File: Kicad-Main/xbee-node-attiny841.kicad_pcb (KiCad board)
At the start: 2 copper layers, 58.5 x 58.5 mm, 41 parts, among them P10 CONN_1, P11 CONN_1, P12 CONN_1, P13 CONN_1, P14 CONN_1, P15 CONN_1, P16 CONN_1, P17 CONN_1, P18 CONN_1, P2 XBee Adaptor, P3 Test, P4 Battery, P5 XBee-ext-1, P6 XBee-ext-2, P7 CONN_1, P8 CONN_1, P9 CONN_1, Q2 S9014, Q3 2N7000, U1 ATTINY84-S, U2 MAX952ESA, U3 TPS77033

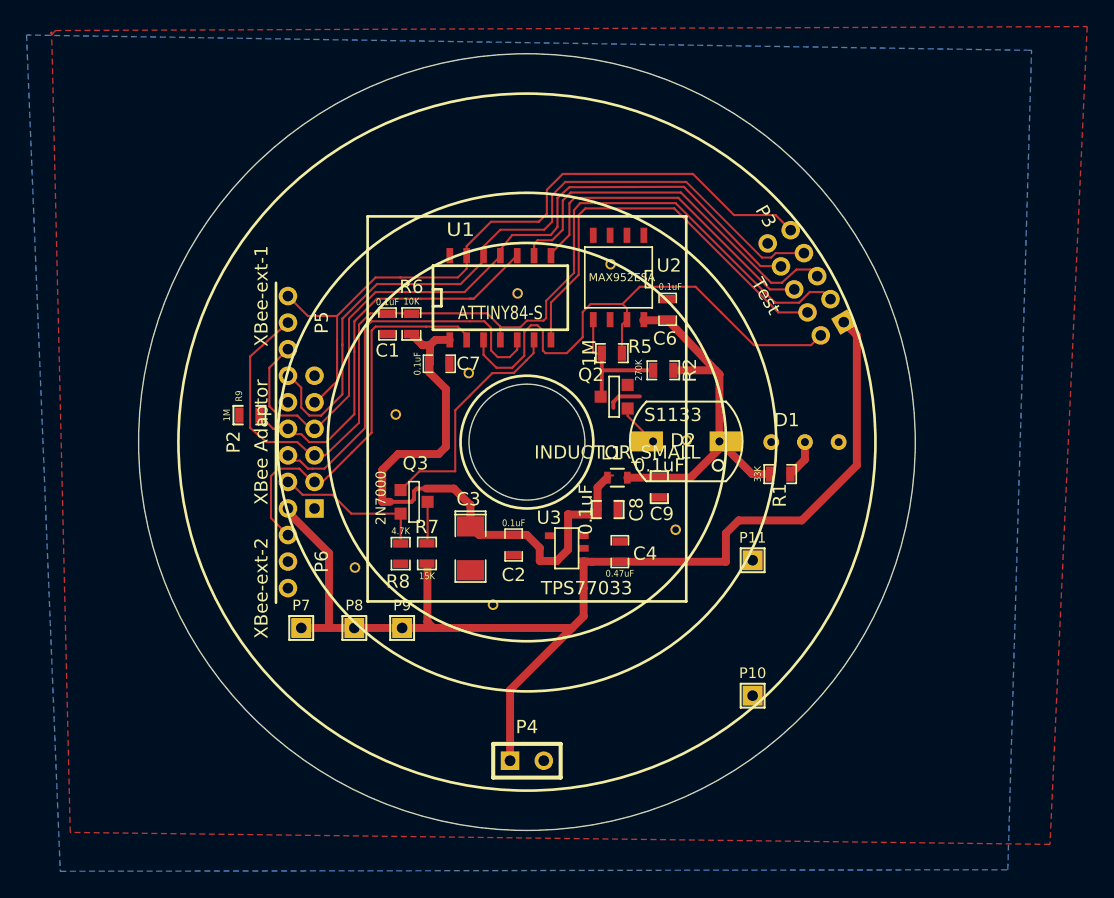
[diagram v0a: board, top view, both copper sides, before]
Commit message: Move some components away from centre to leave room for a shaft housing.
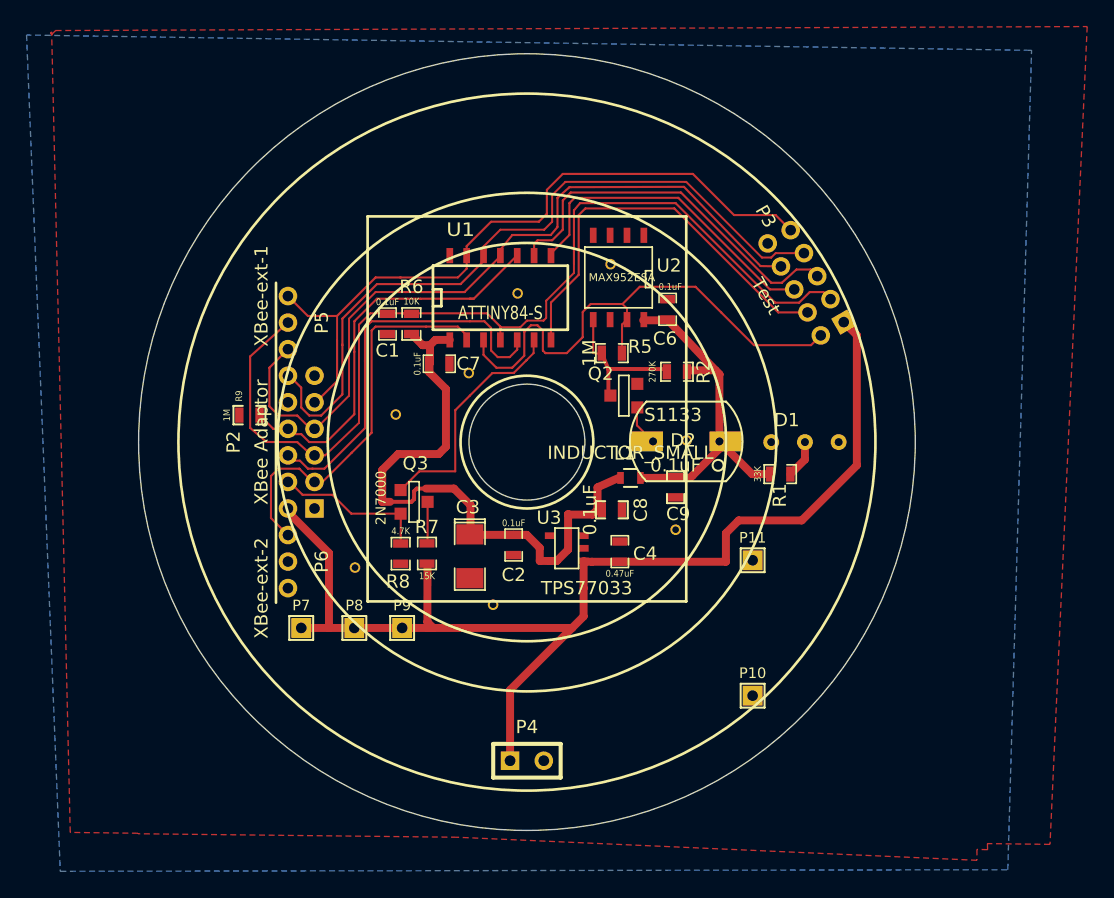
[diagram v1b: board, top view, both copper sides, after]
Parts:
- moved C9 1.23 mm to (211.2, 103.4)
- moved R2 1.04 mm to (211.3, 94.7)
- moved L1 0.99 mm to (207.8, 102.7)
- moved Q2 0.73 mm to (207.3, 96.5)
- moved C3 0.60 mm to (195.7, 108.6)
- moved C8 0.32 mm to (206.4, 105.1)
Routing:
- net (no net): track 2.61 -> 0.00 mm
- net /VDDA: track 29.4 -> 27.1 mm
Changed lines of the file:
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@@
-(kicad_pcb (version 4) (host pcbnew "(2014-08-05 BZR 5054)-product")
+(kicad_pcb (version 4) (host pcbnew 4.0.2-4+6225~38~ubuntu14.04.1-stable)
   (general
     (links 85)
-    (no_connects 5)
-    (area 170.699999 70.699999 229.300001 129.300001)
+    (no_connects 6)
+    (area 162.31 68.7 242.200001 132.330001)
     (thickness 1.6)
     (drawings 11)
-    (tracks 336)
+    (tracks 332)
     (zones 0)
     (modules 41)
@@
   )
   (setup
-    (last_trace_width 0.3)
+    (last_trace_width 0.16)
     (user_trace_width 0.3)
     (user_trace_width 0.6)
@@
   )
   (module SMD_Packages:SM1206POL (layer F.Cu)
-    (at 195.75 108 270)
+    (at 195.7 108.6 270)
     (attr smd)
     (fp_text reference C3 (at -3.7 0.15 360) (layer F.SilkS)
@@
   )
   (module SMD_Packages:SM0603_Resistor (layer F.Cu)
-    (at 210.27 94.59 180)
+    (at 211.3 94.7 180)
     (attr smd)
     (fp_text reference R2 (at -2 0 270) (layer F.SilkS)
@@
   )
   (module SMD_Packages:SOT23EBC (layer F.Cu)
-    (at 206.57 96.58 270)
+    (at 207.3 96.5 270)
     (descr "Module CMS SOT23 Transistore EBC")
     (tags "CMS SOT")
@@
   )
   (module SMD_Packages:SMD-0603_c (layer F.Cu)
-    (at 206.08 105.08)
+    (at 206.4 105.1)
     (attr smd)
     (fp_text reference C8 (at 2.17 0 90) (layer F.SilkS)
@@
   )
   (module SMD_Packages:SMD-0603_c (layer F.Cu)
-    (at 209.97 103.4 270)
+    (at 211.2 103.4 270)
     (attr smd)
     (fp_text reference C9 (at 2.01 -0.19 360) (layer F.SilkS)
@@
   )
   (module Resistors_SMD:R_0603 (layer F.Cu)
-    (at 206.81 102.68 180)
+    (at 207.8 102.7 180)
     (descr "Resistor SMD 0603, reflow soldering, Vishay (see dcrcw.pdf)")
     (tags "resistor 0603")
@@
   (gr_line (start 188 112) (end 212 112) (angle 90) (layer F.SilkS) (width 0.2))
   (gr_circle (center 200 100) (end 204.25 101) (layer Edge.Cuts) (width 0.1))
-  (segment (start 208.51 96.56) (end 206.93 96.56) (width 0.3) (layer F.Cu) (net 0))
-  (segment (start 206.51 96.98) (end 206.51 97.42) (width 0.3) (layer F.Cu) (net 0))
-  (segment (start 206.93 96.56) (end 206.51 96.98) (width 0.3) (layer F.Cu) (net 0))
   (segment (start 184 103) (end 183.86 103) (width 0.16) (layer F.Cu) (net 1))
   (segment (start 183.86 103) (end 182.86 102) (width 0.16) (layer F.Cu) (net 1))
@@
   (segment (start 192.7 92.7) (end 192.138 92.7) (width 0.6) (layer F.Cu) (net 12))
   (segment (start 205.318 105.08) (end 205.318 103.41) (width 0.6) (layer F.Cu) (net 12))
-  (segment (start 205.318 103.41) (end 206.048 102.68) (width 0.6) (layer F.Cu) (net 12))
+  (segment (start 205.318 103.41) (end 206.9 102.7) (width 0.6) (layer F.Cu) (net 12))
   (segment (start 203.1 105.46) (end 204.938 105.46) (width 0.6) (layer F.Cu) (net 12))
   (segment (start 204.938 105.46) (end 205.318 105.08) (width 0.6) (layer F.Cu) (net 12))
-  (segment (start 206 102.512) (end 206.5 102.512) (width 0.15) (layer F.Cu) (net 12))
   (segment (start 203.1 108.1) (end 203.1 105.46) (width 0.6) (layer F.Cu) (net 12))
   (segment (start 203.1 105.46) (end 203.1 105.412) (width 0.6) (layer F.Cu) (net 12))
@@
   (segment (start 195.738 104.738) (end 194.5 103.5) (width 0.6) (layer F.Cu) (net 12))
   (segment (start 195.75 104.738) (end 195.738 104.738) (width 0.6) (layer F.Cu) (net 12))
-  (segment (start 205.638 94.61) (end 205.638 96.846) (width 0.3) (layer F.Cu) (net 13))
-  (segment (start 205.638 93.3) (end 205.638 94.61) (width 0.3) (layer F.Cu) (net 13))
+  (segment (start 206.138 94.51) (end 206.138 96.746) (width 0.3) (layer F.Cu) (net 13))
+  (segment (start 205.638 93.3) (end 206.138 94.51) (width 0.3) (layer F.Cu) (net 13))
   (segment (start 205.47 93.35) (end 204.99 93.29) (width 0.16) (layer F.Cu) (net 13))
   (segment (start 204.99 93.29) (end 204.995 90.775) (width 0.16) (layer F.Cu) (net 13))
   (segment (start 205.47 93.35) (end 205.638 93.3) (width 0.15) (layer F.Cu) (net 13))
-  (segment (start 205.638 94.59) (end 205.658 94.61) (width 0.3) (layer F.Cu) (net 13))
-  (segment (start 205.658 94.61) (end 205.7 94.61) (width 0.3) (layer F.Cu) (net 13))
-  (segment (start 205.7 94.61) (end 205.638 94.61) (width 0.3) (layer F.Cu) (net 13))
-  (segment (start 209.508 94.59) (end 205.638 94.59) (width 0.3) (layer F.Cu) (net 13))
+  (segment (start 206.138 94.49) (end 206.158 94.51) (width 0.3) (layer F.Cu) (net 13))
+  (segment (start 206.158 94.51) (end 206.2 94.51) (width 0.3) (layer F.Cu) (net 13))
+  (segment (start 206.2 94.51) (end 206.138 94.51) (width 0.3) (layer F.Cu) (net 13))
+  (segment (start 210.4 94.5) (end 206.138 94.49) (width 0.3) (layer F.Cu) (net 13))
   (segment (start 203.9 87.4) (end 203.9 82.9) (width 0.16) (layer F.Cu) (net 15))
   (segment (start 203.9 82.9) (end 204.4 82.4) (width 0.16) (layer F.Cu) (net 15))
@@
   (segment (start 220.94 101.312) (end 219.842 102.41) (width 0.6) (layer F.Cu) (net 25))
   (segment (start 220.94 100) (end 220.94 101.312) (width 0.6) (layer F.Cu) (net 25))
-  (segment (start 207.586 98.036) (end 209.5 99.95) (width 0.16) (layer F.Cu) (net 26))
-  (segment (start 207.586 97.469) (end 207.586 98.036) (width 0.16) (layer F.Cu) (net 26))
-  (segment (start 207.56 102.68) (end 212.32 102.68) (width 0.6) (layer F.Cu) (net 27))
+  (segment (start 208.286 98.736) (end 209.5 99.95) (width 0.16) (layer F.Cu) (net 26))
+  (segment (start 208.286 97.369) (end 208.286 98.736) (width 0.16) (layer F.Cu) (net 26))
+  (segment (start 208.7 102.7) (end 212.32 102.68) (width 0.6) (layer F.Cu) (net 27))
   (segment (start 212.488 102.512) (end 214.5 100.5) (width 0.6) (layer F.Cu) (net 27))
   (segment (start 212.32 102.68) (end 212.488 102.512) (width 0.6) (layer F.Cu) (net 27))
@@
   (segment (start 208.755 90.825) (end 210.625 90.825) (width 0.6) (layer F.Cu) (net 27))
   (segment (start 218.318 102.41) (end 216.96 102.41) (width 0.6) (layer F.Cu) (net 27))
-  (segment (start 211.032 94.59) (end 214.19 94.59) (width 0.6) (layer F.Cu) (net 27))
+  (segment (start 212.2 94.6) (end 214.19 94.59) (width 0.6) (layer F.Cu) (net 27))
   (segment (start 214.19 94.59) (end 214.5 94.9) (width 0.6) (layer F.Cu) (net 27))
   (segment (start 210.625 90.825) (end 214.5 94.9) (width 0.6) (layer F.Cu) (net 27))
@@
     (polygon
       (pts
-        (xy 242.2 68.7) (xy 239.4 130.3) (xy 165.6 129.4) (xy 164.204538 69.295462) (xy 164.5 69)
+        (xy 239.4 130.3) (xy 234.68425 130.242491) (xy 234.7 130.7) (xy 233.893371 130.679379) (xy 233.9 131.5)
+        (xy 194.734053 129.763284) (xy 170.7 129.5) (xy 170.698854 129.462181) (xy 165.6 129.4) (xy 164.204538 69.295462)
+        (xy 164.5 69) (xy 242.2 68.7) (xy 239.4 130.3)
       )
     )

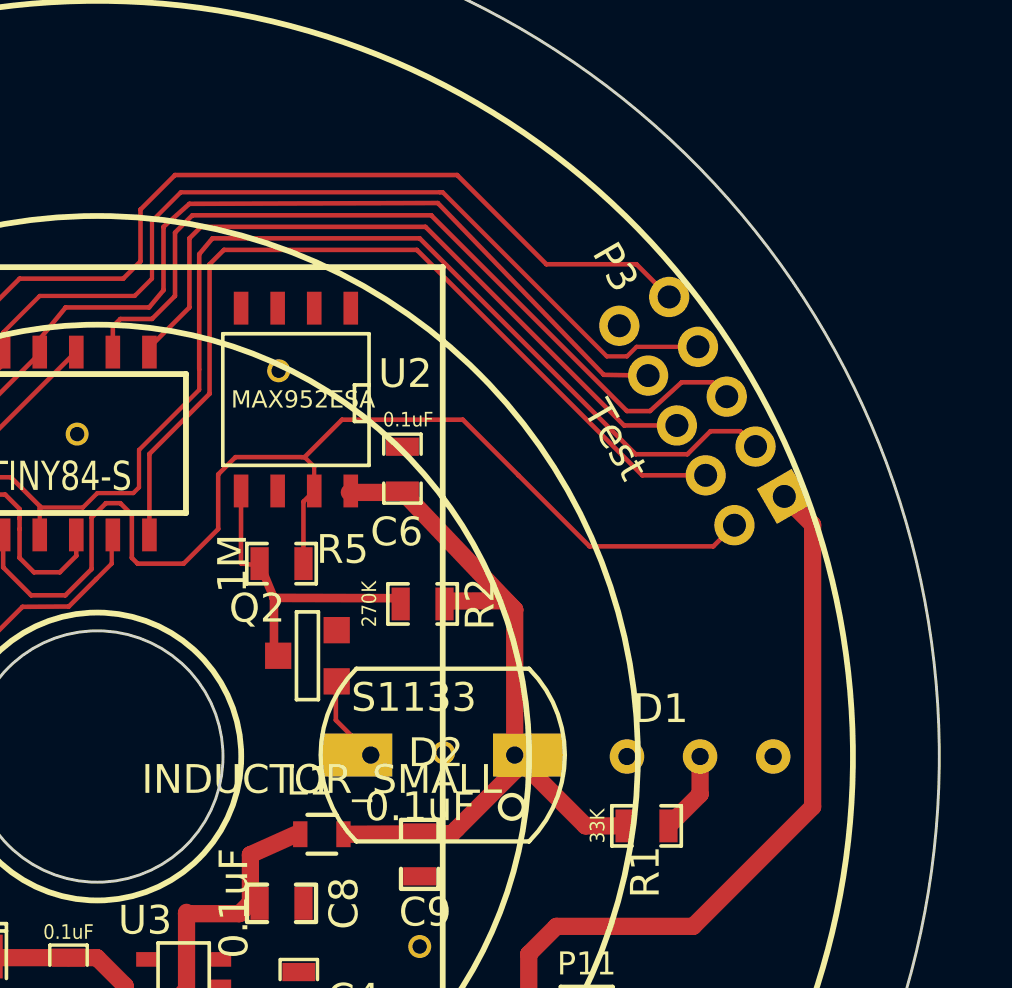
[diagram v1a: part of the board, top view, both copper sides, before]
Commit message: Change orientation of debug connector on main board to fit in housing. Update mounts to narrow down the LED mount
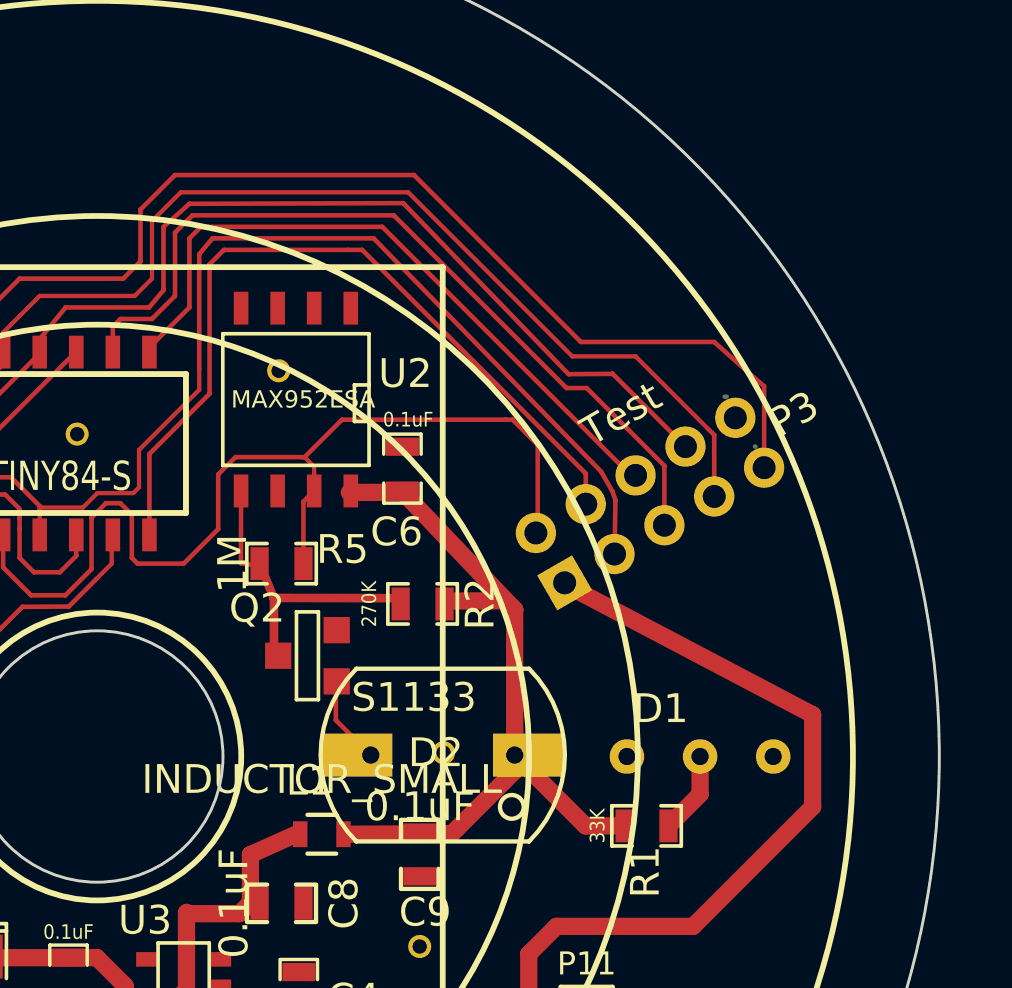
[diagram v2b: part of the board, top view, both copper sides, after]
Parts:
- moved P3 3.58 mm to (219.2, 91.1), turned to 30 degrees
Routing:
- net /On/Sleep: track 54.1 -> 61.4 mm
- net /Count: track 40.5 -> 34.6 mm
- net /Tx: track 55.9 -> 59.6 mm
- net /MOSI: track 31.0 -> 27.9 mm
- net /Reset: track 75.0 -> 72.4 mm
- net /Rx: track 59.4 -> 61.8 mm
- net /Battery: track 90.2 -> 91.7 mm

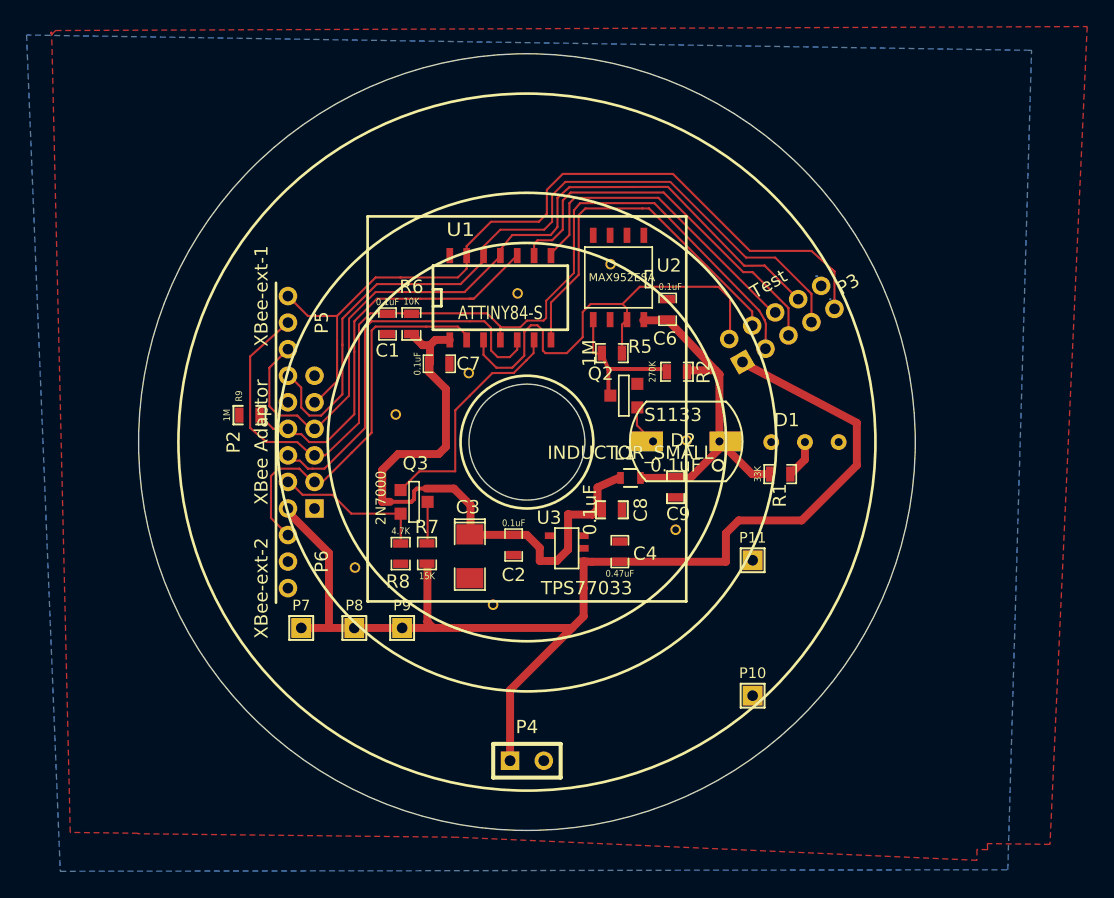
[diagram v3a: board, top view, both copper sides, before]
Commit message: Shift XBee connector on main board by 1mm to avoid housing structures. Update documentation.
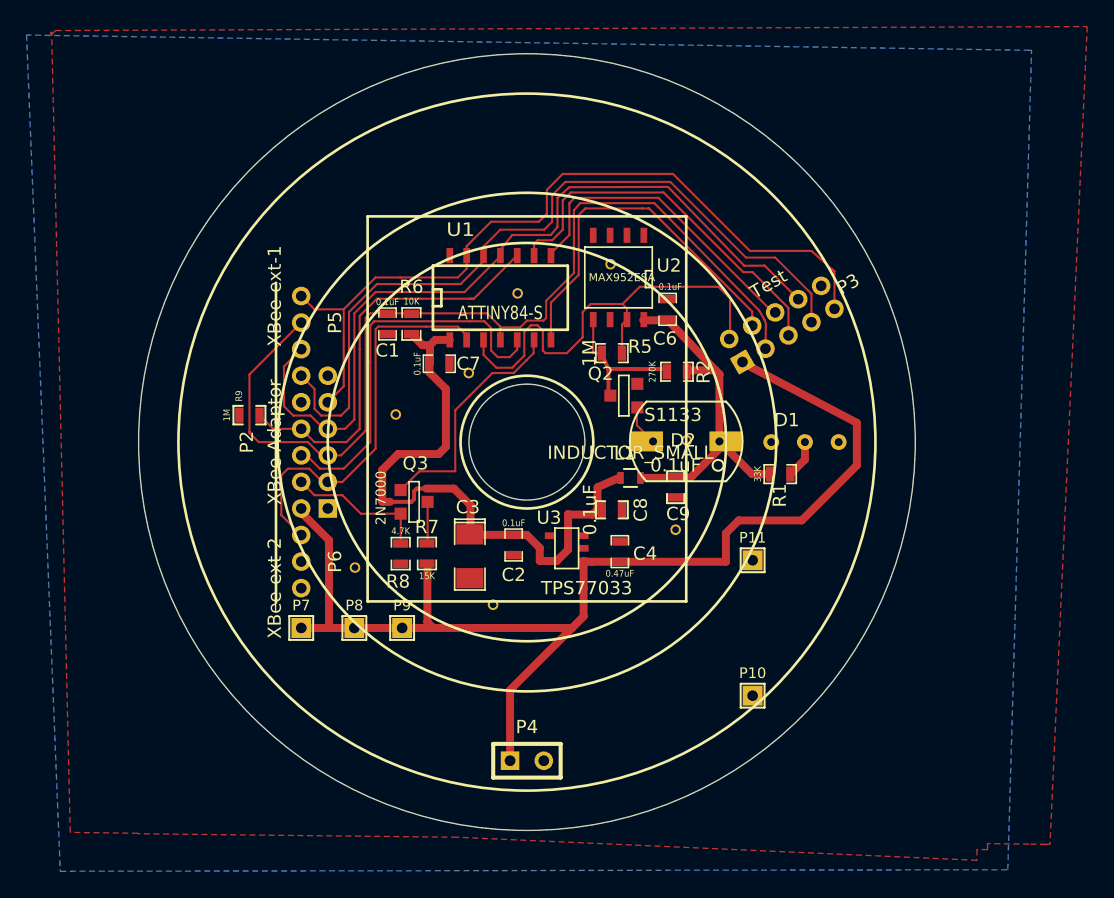
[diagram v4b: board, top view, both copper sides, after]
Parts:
- moved P2 1.00 mm to (184.0, 100.0)
- moved P5 1.00 mm to (183.0, 91.0)
- moved P6 1.00 mm to (183.0, 109.0)
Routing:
- net /Reset: track 72.4 -> 73.8 mm
- net /On/Sleep: track 61.4 -> 60.3 mm
- net /VBatt: track 11.9 -> 10.9 mm
- net /Sleep-Rq: track 30.4 -> 31.4 mm
- net /Battery: track 91.7 -> 91.1 mm
- net /Xbee-Reset: track 29.7 -> 29.1 mm
